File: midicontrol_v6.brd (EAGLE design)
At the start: 118.5 x 42.7 mm, 67 parts, among them SW1 EC12E_SW, U1 6N138S(TB), U3 74HC595D, U4 ATMEGA328P-AN, Y1 CSTCE16M0V53-R0

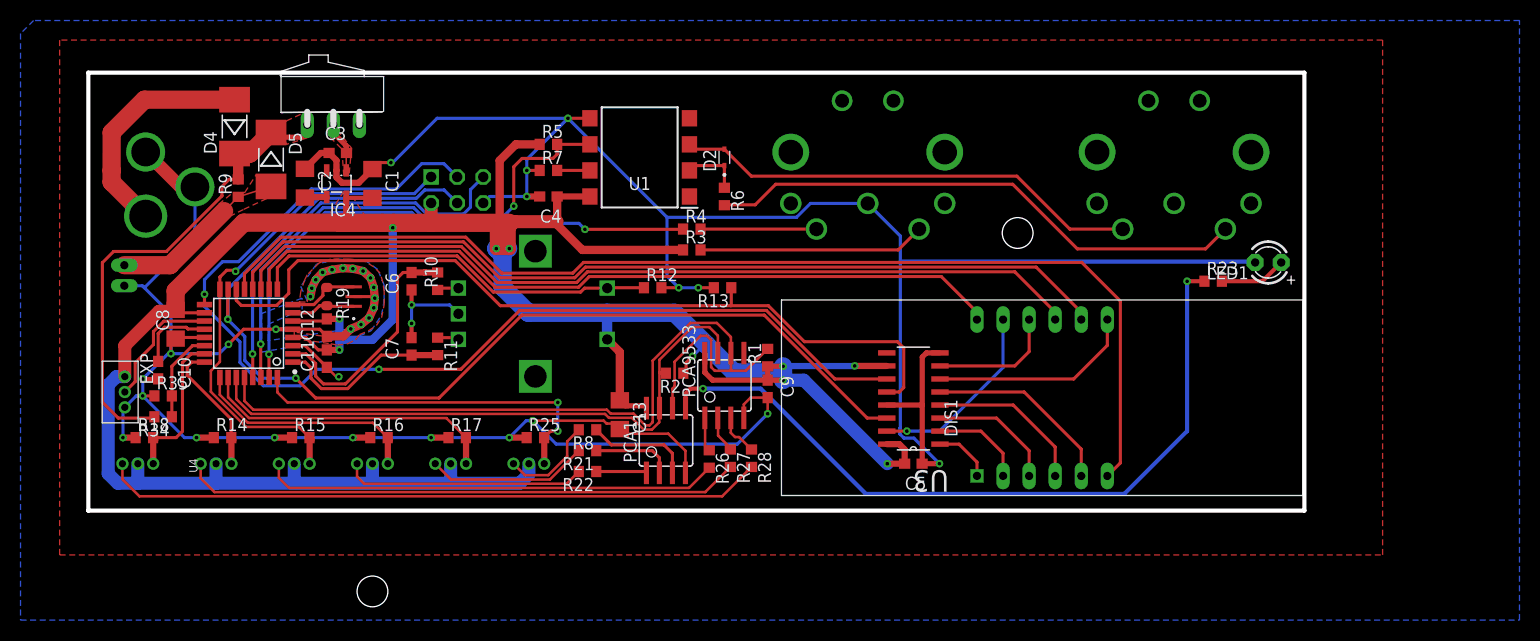
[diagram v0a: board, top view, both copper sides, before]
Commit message: finished midiconrol
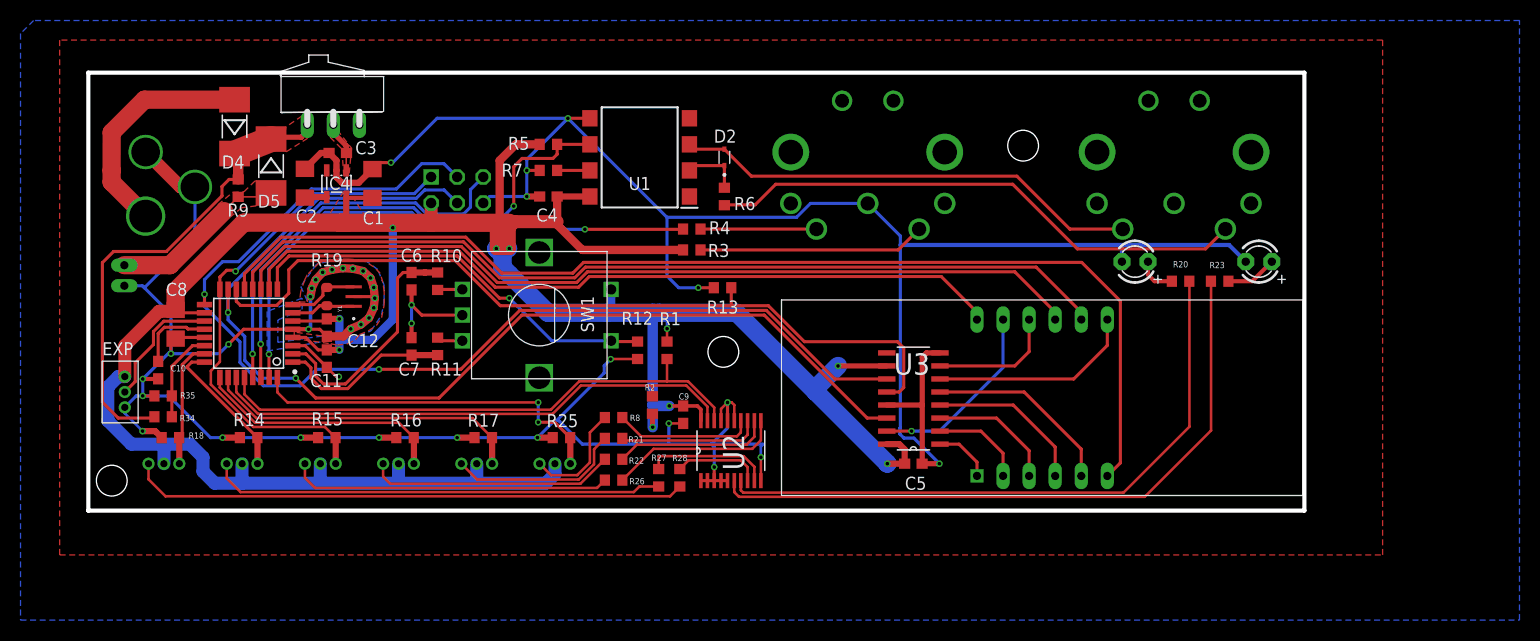
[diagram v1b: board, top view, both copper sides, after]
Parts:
- removed C13: 0.1uf, rcl:C1206
- removed PCA1: PCA9533/02, adam - ics:SOIC8
- removed PCA9533: PCA9533/01, adam - ics:SOIC8
- added LED2: (no value), adafruit:LED3MM
- added R20: 220R, rcl:R0603
- added U2: PCA9634PW,112, PCA9634PW_112:SOP65P640X110-20N
- moved R1 9.83 mm to (55.4, 73.3), turned to 270 degrees
- moved R26 9.55 mm to (50.2, 60.6), turned to 180 degrees
- moved C9 8.61 mm to (56.9, 67.0)
- moved R27 7.24 mm to (54.6, 60.9)
- moved R28 7.24 mm to (56.6, 60.9)
- moved R12 6.27 mm to (52.5, 73.3), turned to 270 degrees
- moved R2 3.78 mm to (53.9, 67.9), turned to 90 degrees
- moved R8 2.81 mm to (50.2, 66.7)
- moved R21 2.81 mm to (50.2, 64.7)
- moved R22 2.81 mm to (50.2, 62.7)
- moved BTN_5 2.54 mm to (44.5, 62.2)
- moved R17 2.54 mm to (37.5, 64.8)
- moved R15 2.54 mm to (22.2, 64.8)
- moved BTN_1 2.54 mm to (14.0, 62.2)
- moved R14 2.54 mm to (14.6, 64.8)
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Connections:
- new net N$31: R20.1, U2.7
- new net N$32: R23.1, U2.6
- net +5V: now also U2.20; no longer C13.1, PCA1.8, PCA9533.8
- net ENC_A: now also SW1.A; no longer SW1.B
- net ENC_B: now also SW1.B; no longer SW1.A
- net GND: now also LED2.K, U2.1, U2.10, U2.15, U2.16, U2.17, U2.2, U2.3, U2.4, U2.5; no longer C13.2, PCA1.4, PCA9533.4
- net N$22: now also LED2.A, R20.2; no longer PCA9533.3, R28.1
- net N$23: now also R8.1, U2.14; no longer PCA9533.2, R27.1
- net N$24: now also R21.1, U2.13; no longer PCA9533.1, R26.1
- net N$27: now also R22.1, U2.12; no longer PCA1.2, R21.1
- net N$28: now also R26.1, U2.11; no longer PCA1.3, R8.1
- net N$29: now also R27.1, U2.9; no longer PCA1.1, R22.1
- net N$30: now also R28.1, U2.8; no longer PCA1.5, R23.1
- net SCL: now also U2.18; no longer PCA1.6, PCA9533.6
- net SDA: now also U2.19; no longer PCA1.7, PCA9533.7
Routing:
- net N$30: track 73.6 -> 8.55 mm, vias 2 -> 0
- net N$32: track 0.00 -> 65.0 mm
- net N$31: track 0.00 -> 61.6 mm
- net SCL: track 80.7 -> 53.7 mm
- net GND: track 372.0 -> 388.7 mm, vias 38 -> 40
- net LED_GND_0: track 44.5 -> 31.3 mm
- net +5V: track 289.2 -> 278.0 mm
- net N$24: track 3.34 -> 13.9 mm
- net LED_GND_2: track 64.7 -> 54.4 mm
- net LED_GND_1: track 54.6 -> 44.3 mm
- net N$23: track 3.59 -> 13.6 mm
- net SDA: track 60.6 -> 52.7 mm
- net N$27: track 7.91 -> 15.3 mm
- net N$29: track 4.94 -> 12.4 mm
- net N$28: track 10.3 -> 17.0 mm
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
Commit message: finalized it
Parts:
- added TP1, TP2, TP3: TPSQTP18R, testpad:TP18R
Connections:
- net B3: now also TP1.TP
- net B4: now also TP2.TP
- net GND: now also TP3.TP
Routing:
- net GND: track 388.7 -> 458.0 mm, vias 40 -> 49
- net B4: track 31.4 -> 34.0 mm
- net B3: track 24.4 -> 27.1 mm
- net B5: track 35.5 -> 36.4 mm
- net B2: track 14.2 -> 14.9 mm

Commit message: changed xh to ph pins
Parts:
- removed BTN_0, BTN_1, BTN_2, BTN_3, BTN_4, BTN_5: B3B-ZR, jst:B3B-ZR
- added BTN0, BTN1, BTN2, BTN3, BTN4, BTN5: B3B-PH-K, con-jst-ph:B3B-PH-K
- EXP: value B3B-ZR -> B3B-PH-K; device jst:B3B-ZR -> con-jst-ph:B3B-PH-K
- R35: value 69k -> 125k
- moved R2 9.73 mm to (63.6, 69.4), turned to 180 degrees
- moved U2 9.61 mm to (71.1, 64.8)
- moved R21 8.26 mm to (58.4, 64.7)
- moved R22 8.26 mm to (58.4, 62.7)
- moved R26 8.26 mm to (58.4, 60.6)
- moved R8 8.26 mm to (58.4, 66.7)
- moved C9 7.83 mm to (64.8, 67.3), turned to 180 degrees
- moved R27 7.62 mm to (62.2, 60.9)
- moved R28 7.62 mm to (64.2, 60.9)
- moved TP2 7.01 mm to (47.6, 62.9)
- moved TP1 5.75 mm to (38.7, 62.9)
- moved R25 5.71 mm to (50.8, 64.8)
- moved TP3 4.49 mm to (29.8, 62.9)
- moved R17 3.81 mm to (41.3, 64.8)
- moved R16 3.18 mm to (33.0, 64.8)
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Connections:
- net +5V: now also BTN0.2, BTN1.2, BTN2.2, BTN3.2, BTN4.2, BTN5.2; no longer BTN_0.2, BTN_1.2, BTN_2.2, BTN_3.2, BTN_4.2, BTN_5.2
- net B1: now also BTN0.1; no longer BTN_0.1
- net B2: now also BTN1.1; no longer BTN_1.1
- net B3: now also BTN3.1; no longer BTN_3.1
- net B4: now also BTN4.1; no longer BTN_4.1
- net B5: now also BTN5.1; no longer BTN_5.1
- net LED_GND_0: now also BTN2.3; no longer BTN_2.3
- net LED_GND_1: now also BTN1.3; no longer BTN_1.3
- net LED_GND_2: now also BTN0.3; no longer BTN_0.3
- net LED_GND_4: now also BTN5.3; no longer BTN_5.3
- net LED_GND_5: now also BTN4.3; no longer BTN_4.3
- net LED_GND_6: now also BTN3.3; no longer BTN_3.3
- net MISO: now also BTN2.1; no longer BTN_2.1
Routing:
- net GND: track 458.0 -> 480.3 mm
- net SDA: track 52.7 -> 62.4 mm
- net SCL: track 53.7 -> 62.8 mm
- net N$32: track 65.0 -> 56.1 mm
- net N$31: track 61.6 -> 52.7 mm
- net B5: track 36.4 -> 43.8 mm
- net B4: track 34.0 -> 40.5 mm
- net LED_GND_2: track 54.4 -> 60.3 mm
- net B3: track 27.1 -> 32.6 mm
- net LED_GND_1: track 44.3 -> 49.0 mm
- net LED_GND_0: track 31.3 -> 35.5 mm
- net MISO: track 52.4 -> 56.1 mm
- net +5V: track 278.0 -> 281.5 mm, vias 10 -> 9
- net N$30: track 8.55 -> 11.6 mm
- net LED_GND_6: track 24.1 -> 27.1 mm
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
